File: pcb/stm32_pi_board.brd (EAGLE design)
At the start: 84 x 56 mm, 67 parts, among them IC1 LD1117, IC2 ESP-11, IC3 LD1117, IC4 STM32F405RG, IC5 STF203-22, Q1 BSH205, Q2 N2004, Q5 BSH205, Q6 N2004, X1 PJ-043-SMT, X2 DM3AT, X3 XM7D-0512

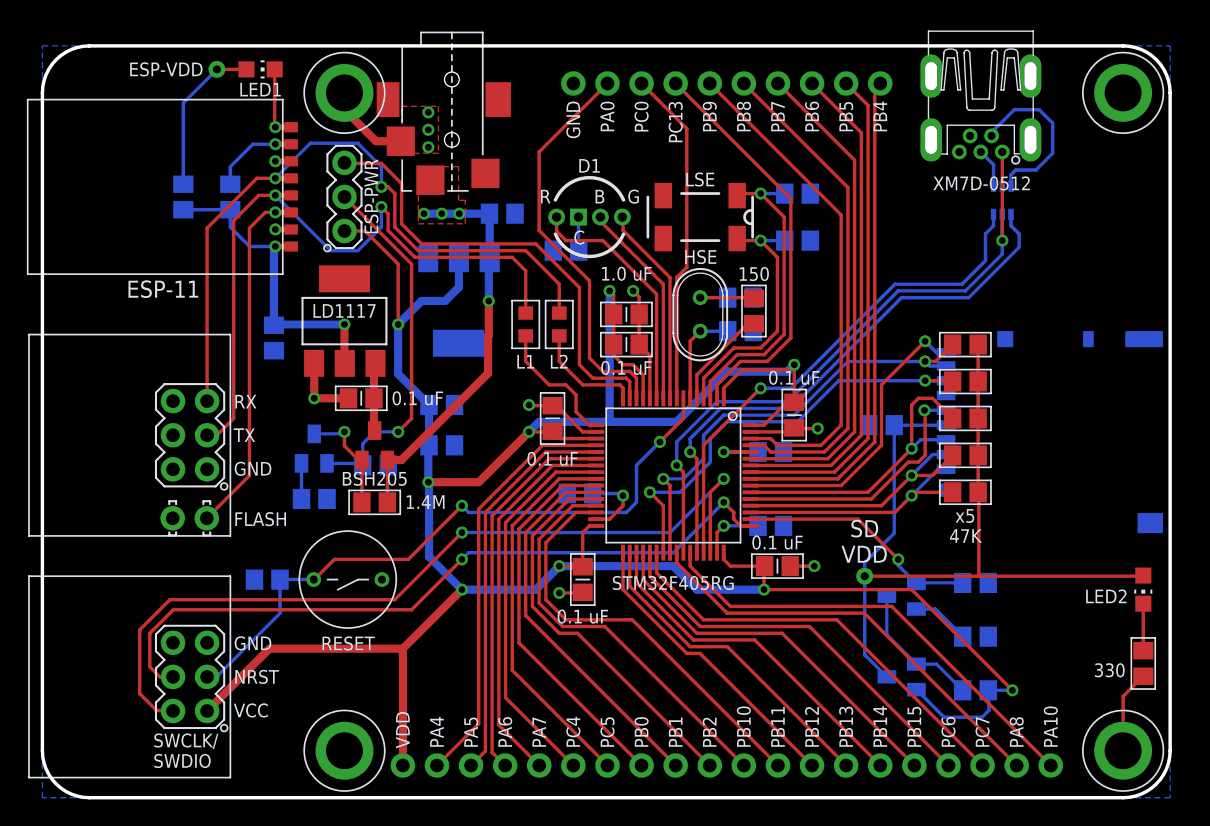
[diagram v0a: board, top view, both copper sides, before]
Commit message: Imprved stm32_pi_board
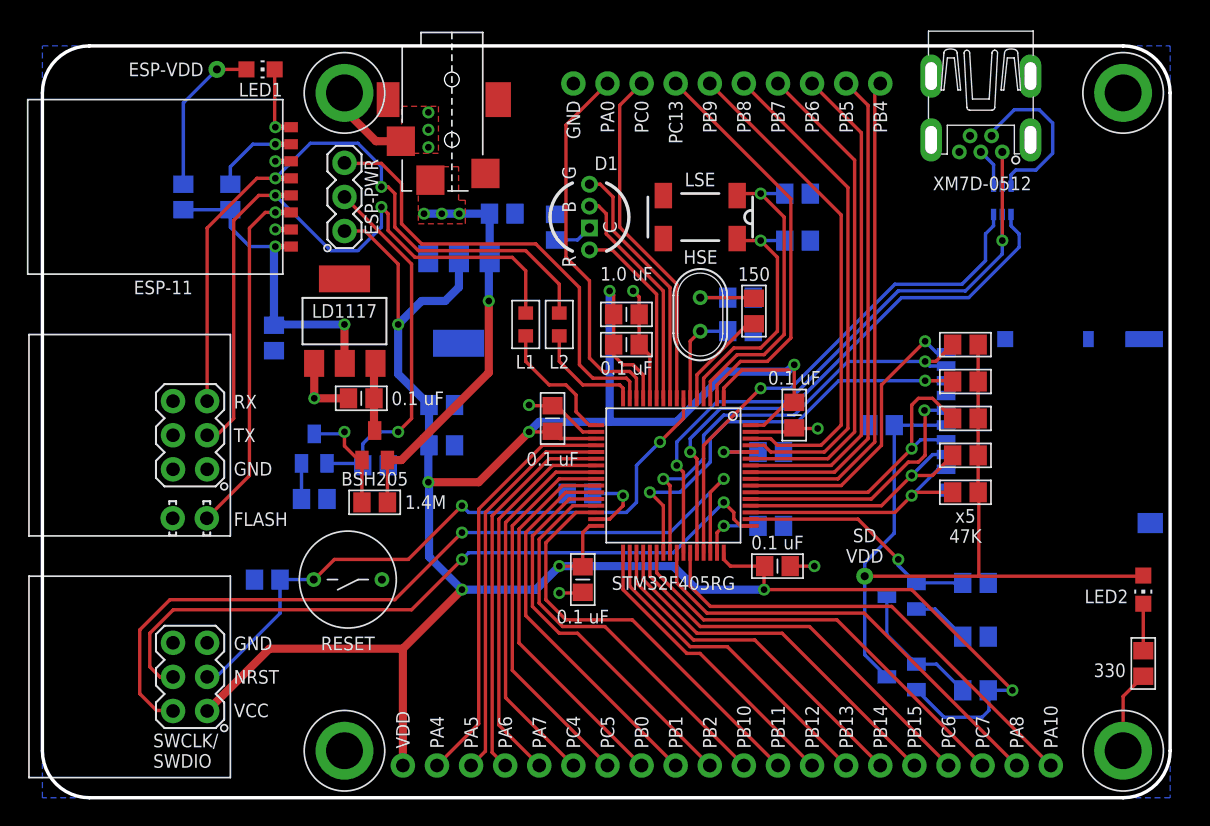
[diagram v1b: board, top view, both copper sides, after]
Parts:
- IC1, IC3: device burr-brown:SOT223 -> MyComponents:SOT223
- SV1, SV2: value (none) -> 75867-331LF
- SV4: value (none) -> 68000-420HLF
- SV5: value (none) -> 69190-410HLF
- moved R6 1.90 mm to (38.2, 42.5), turned to 90 degrees
- turned D1 to 90 degrees
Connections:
- net BOOT1 renamed BOOT
- net N$42 renamed D1_BLUE
- net N$43 renamed D1_RED
- net N$44 renamed D1_GREEN
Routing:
- net D1_RED: track 18.2 -> 14.1 mm
- net D1_GREEN: track 15.0 -> 18.9 mm
- net PA0: track 29.7 -> 28.1 mm
- net D1_BLUE: track 15.5 -> 17.0 mm
- net PA8: track 32.3 -> 33.2 mm
- net PA10: track 34.0 -> 34.9 mm
- net PC0: track 25.2 -> 25.9 mm

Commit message: STM32-Pi Board submitted to factory
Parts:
- moved X3 3.00 mm to (72.9, 49.0)
- moved IC5 1.40 mm to (72.9, 44.5)
- moved SV4 0.50 mm to (51.0, 2.90)
- moved SV5 0.10 mm to (51.0, 53.1)
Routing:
- net N$36: track 12.8 -> 6.27 mm
- net USB-VBUS: track 48.1 -> 49.5 mm
- net USB-DM: track 41.8 -> 42.7 mm
- net USB-DP: track 38.4 -> 38.9 mm
- net PA5: track 29.4 -> 28.9 mm
- net PA4: track 31.1 -> 30.6 mm
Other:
- board text added: "STM32-Pi Board Revision 1.0 (C) Mikhail Kulesh, 2017"

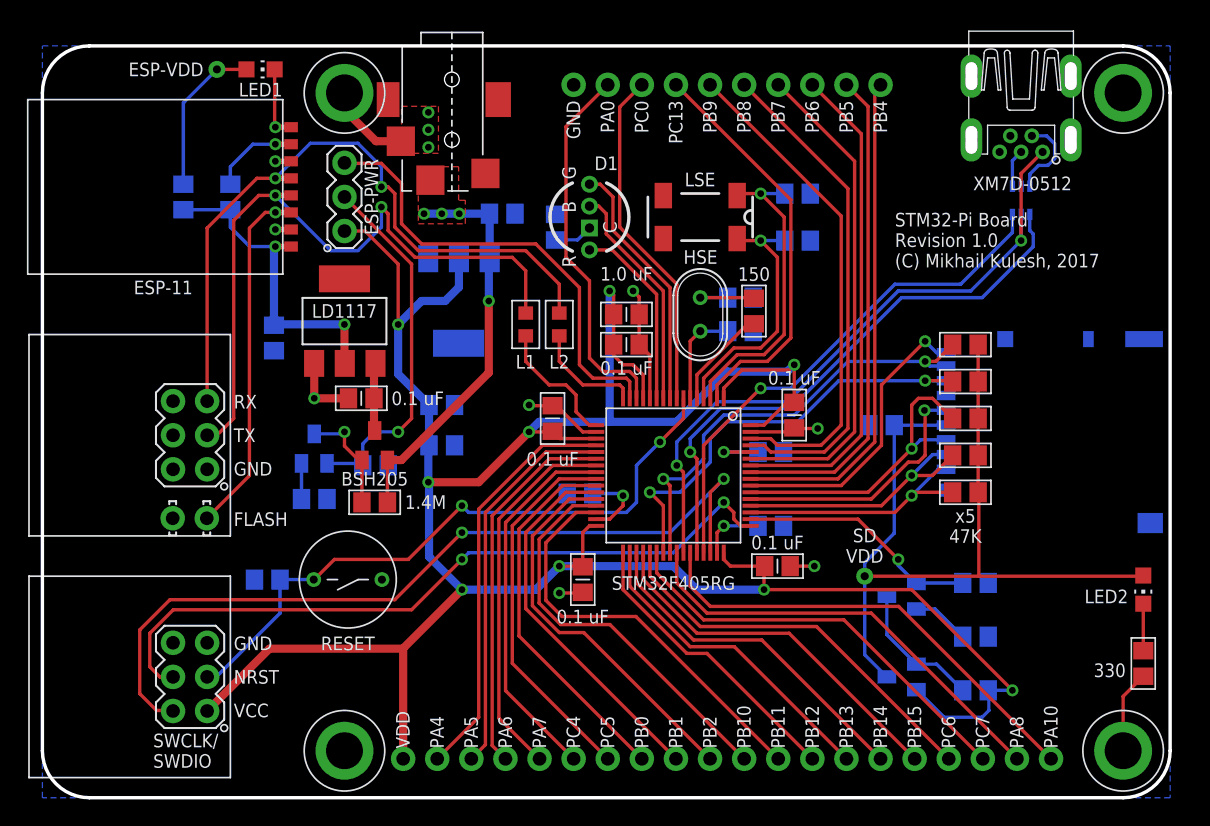
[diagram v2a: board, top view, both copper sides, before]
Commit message: Fixed minor layout bugs
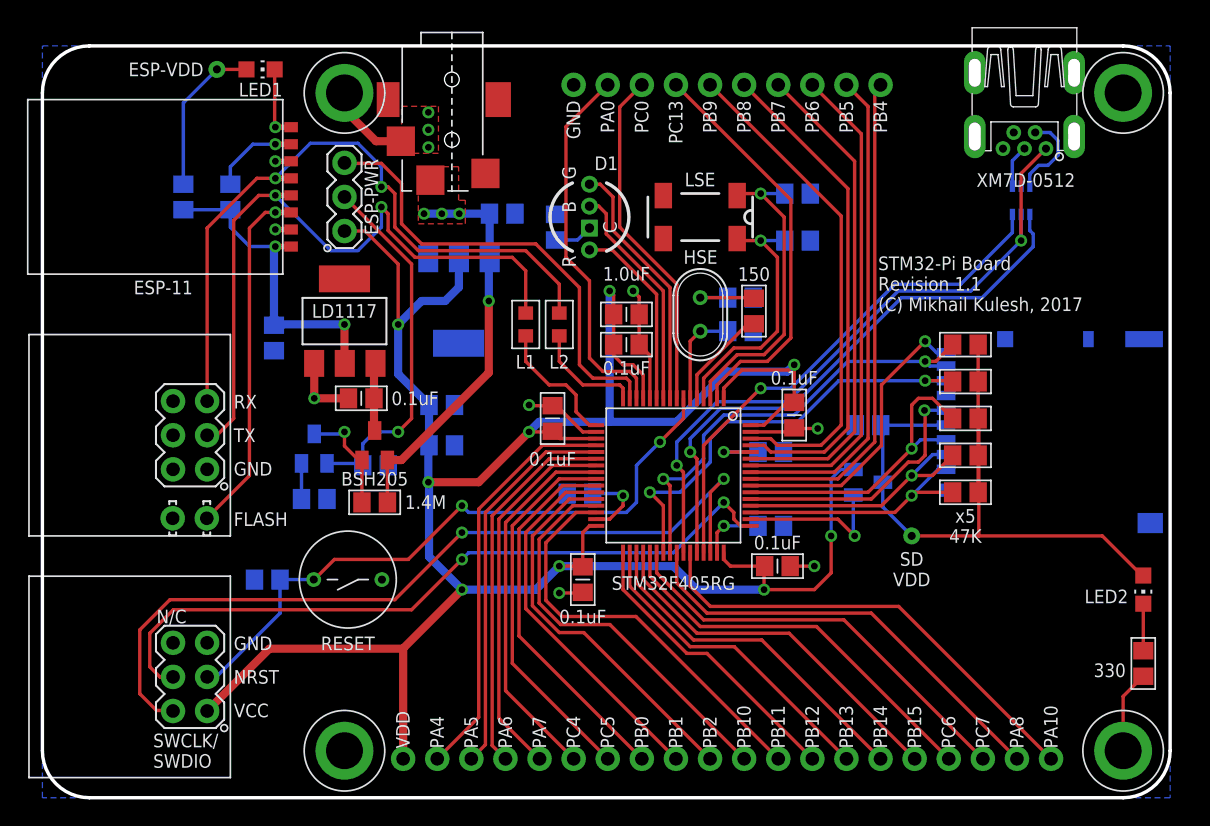
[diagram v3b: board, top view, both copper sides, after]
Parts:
- removed Q6: N2004, MyComponents:SOT23
- removed R11: 330K, MyComponents:R0805
- removed R12: 10K, MyComponents:R0805
- removed R9: 1.4M, MyComponents:R0805
- C10, C11, C12, C16, C19, C2, C6, C8, C9: value 0.1 uF -> 0.1uF
- C13: value 1.0 uF -> 1.0uF
- C17, C18: value 2.2 uF -> 2.2uF
- C3, C7: value 10 uF -> 10uF
- moved Q5 14.7 mm to (61.5, 23.5), turned to 90 degrees
- moved C19 1.00 mm to (61.5, 27.8)
- moved X3 0.35 mm to (73.2, 49.2)
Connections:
- removed net D_VG: Q5.1, Q6.3, R9.1
- removed net N$136: Q6.2, R12.2
- net GND: no longer R11.1, R12.1
- net SD-ON: now also Q5.1; no longer Q6.1, R11.2
- net VDD: no longer R9.2
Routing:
- net VDD: track 205.3 -> 188.4 mm
- net D_VG: track 10.2 -> 0.00 mm
- net SD-VDD: track 62.3 -> 52.5 mm
- net SD-ON: track 18.1 -> 11.4 mm
- net N$136: track 4.30 -> 0.00 mm
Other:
- board text added: "N/C"
- board text added: "STM32-Pi Board Revision 1.1 (C) Mikhail Kulesh, 2017"
- board text removed: "STM32-Pi Board Revision 1.0 (C) Mikhail Kulesh, 2017"

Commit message: Updated PCB
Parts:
- removed SV5: 69190-410HLF, MyComponents:MA10-1-NO-PL
- added SV3: (no value), MyComponents:MA12-1-NO-PL
- moved SV4 0.50 mm to (51.5, 2.90)
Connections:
- net GND: now also SV3.2; no longer SV5.1
- net PA0: now also SV3.3; no longer SV5.2
- net PB4: now also SV3.11; no longer SV5.10
- net PB5: now also SV3.10; no longer SV5.9
- net PB6: now also SV3.9; no longer SV5.8
- net PB7: now also SV3.8; no longer SV5.7
- net PB8: now also SV3.7; no longer SV5.6
- net PB9: now also SV3.6; no longer SV5.5
- net PC0: now also SV3.4; no longer SV5.3
- net PC13: now also SV3.5; no longer SV5.4
- net USB-VBUS: now also SV3.12
- net VIN: now also SV3.1
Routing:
- net VIN: track 31.6 -> 46.3 mm
- net USB-VBUS: track 49.9 -> 64.6 mm
- net ESP-TXI: track 50.7 -> 52.1 mm
- net PB1: track 28.0 -> 29.1 mm
- net PB2: track 29.0 -> 30.0 mm
- net PB10: track 30.1 -> 30.9 mm
- net ESP-RXI: track 51.8 -> 52.5 mm
- net PB11: track 31.2 -> 31.8 mm
- net PC6: track 29.6 -> 30.1 mm
- net PB15: track 27.7 -> 28.2 mm
- net PB14: track 25.9 -> 26.4 mm
- net PB13: track 24.0 -> 24.5 mm
- net PB12: track 22.1 -> 22.6 mm
- net PA8: track 33.0 -> 33.5 mm
- net PA10: track 34.7 -> 35.2 mm
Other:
- board text added: "+3.3V"
- board text added: "+5V"
- board text added: "VBUS"
- board text removed: "VDD"

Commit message: Revision 1.1 submitted to factory
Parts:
- removed ESP-PWR: (no value), MyComponents:MA03-1
- removed IC1: LD1117, MyComponents:SOT223
- removed LED1, LED2: R971, led:CHIP-LED0805
- removed Q1: BSH205, MyComponents:SOT23
- removed Q2: N2004, MyComponents:SOT23
- removed R1: 1.4M, MyComponents:R0805
- removed R2: 330K, MyComponents:R0805
- added ESP-ON, SD-ON: R971, led:CHIP-LED0805
- added IC6: MIC5219-3.3, v-reg-micrel:SOT23-5
- added PWR: (no value), MyComponents:MA03-1
- C2: value 0.1uF -> 470pF
- C3: value 10uF -> 2.2uF
- moved R13 19.2 mm to (82.0, 29.2), turned to 270 degrees
- moved C2 14.3 mm to (12.2, 38.2), flipped to the bottom, turned to 180 degrees
- moved R3 14.0 mm to (12.2, 33.8)
- moved C19 13.3 mm to (74.8, 29.2), flipped to the top, turned to 270 degrees
- moved Q5 13.3 mm to (74.8, 22.0), flipped to the top, turned to 0 degrees
- moved C6 11.9 mm to (23.8, 38.0), flipped to the top, turned to 180 degrees
- moved C3 8.40 mm to (12.2, 41.0), turned to 180 degrees
- moved IC3 8.14 mm to (25.0, 31.5), flipped to the top
- moved C14 3.47 mm to (31.5, 29.2), flipped to the top, turned to 180 degrees
- moved C7 2.85 mm to (31.5, 31.5), flipped to the top, turned to 180 degrees
- moved R5 2.47 mm to (12.2, 46.5), turned to 180 degrees
- moved R4 2.02 mm to (12.2, 43.8), turned to 180 degrees
- moved R6 0.79 mm to (38.0, 43.2)
- moved L1 0.56 mm to (35.8, 34.8)
- moved L2 0.56 mm to (38.2, 34.8)
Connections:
- removed net E_VG: Q1.1, Q2.3, R1.1
- removed net N$148: C2.2, IC1.3, Q1.3
- removed net N$150: Q2.2, R3.2
- new net N$4: C2.2, IC6.4
- net ESP-ON: now also PWR.3; no longer ESP-PWR.3
- net ESP-ON1: now also IC6.3, PWR.2, R3.2; no longer ESP-PWR.2, Q2.1, R2.2
- net ESP-VDD: now also IC6.5; no longer IC1.2
- net GND: now also ESP-ON.C, IC6.2; no longer IC1.1, LED1.C, R2.1
- net N$10: now also ESP-ON.A; no longer LED1.A
- net N$120: now also SD-ON.C; no longer LED2.C
- net SD-VDD: now also SD-ON.A; no longer LED2.A
- net VDD: now also PWR.1; no longer ESP-PWR.1
- net VIN: now also IC6.1; no longer Q1.2, R1.2
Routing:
- net VDD: track 188.6 -> 222.3 mm, vias 9 -> 8
- net GND: track 46.4 -> 68.9 mm, vias 10 -> 9
- net SD-VDD: track 52.5 -> 34.7 mm
- net ESP-ON1: track 27.3 -> 44.5 mm
- net ESP-VDD: track 24.1 -> 13.2 mm, vias 2 -> 1
- net SD-ON: track 11.4 -> 21.2 mm, vias 1 -> 0
- net ESP-ON: track 34.4 -> 43.9 mm
- net E_VG: track 8.25 -> 0.00 mm, vias 1 -> 0
- net VIN: track 46.3 -> 38.3 mm
- net ESP-TXI: track 52.1 -> 44.3 mm, vias 2 -> 1
- net ESP-RXI: track 52.5 -> 45.7 mm, vias 2 -> 1
- net N$148: track 5.07 -> 0.00 mm
- net N$10: track 11.8 -> 15.9 mm
- net N$4: track 0.00 -> 3.51 mm
- net USB-VBUS: track 64.6 -> 68.0 mm
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- removed copper zone on layer 1, net GND
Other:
- board text removed: "ESP-VDD"
- board text removed: "SD VDD"

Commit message: Assembled board 1.2
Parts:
- added C20, C21, C25, C26, C28, C29, C30, C31, C33: 0.1uF, MyComponents:C0805
- added C22: 2.2uF, MyComponents:CPOL0805
- added C23: 470pF, MyComponents:C0805
- added C24, C27, C35, C36, C37: 47uF, MyComponents:CPOL1311
- added C32, C34: 1.0uF, MyComponents:C0805
- added IC1, IC8: MIC5219-3.3, MyComponents:SOT23-5
- added IC7: IS31AP2005, MyComponents:MSOP-8
- added IC9: UDA1334ATS, MyComponents:SSOP16
- added Q1: FDG6332C, MyComponents:SC70-6
- added R1, R2, R20, R21, R9: 150K, MyComponents:R0805
- added R11: 6.7K, MyComponents:R0805
- added R12, R18: 1, MyComponents:R0805
- added R19, R24, R25: 10K, MyComponents:R0805
- added R22, R23: 220K, MyComponents:R0805
- added SV5: (no value), MyComponents:MA04-1
- C3: device MyComponents:C0805 -> MyComponents:CPOL0805
- C6: value 0.1uF -> 470pF
- C7: value 10uF -> 2.2uF; device MyComponents:C0805 -> MyComponents:CPOL0805
- HSE: device MyComponents:HC-46X -> MyComponents:Q-FA-128
- IC3: value LD1117 -> IS31AP2005; device MyComponents:SOT223 -> MyComponents:MSOP-8
- IC6: device v-reg-micrel:SOT23-5 -> MyComponents:SOT23-5
- LSE: device MyComponents:MC-306 -> MyComponents:Q-CM7V-T1A
- R7: value 150 -> 100
- moved C16 63.7 mm to (80.0, 9.00), flipped to the top
- moved SV1 60.5 mm to (71.2, 14.5), turned to 270 degrees
- moved RESET 57.3 mm to (80.0, 14.5)
- moved IC3 26.9 mm to (11.0, 8.50), turned to 90 degrees
- moved L2 19.4 mm to (22.2, 45.8), turned to 0 degrees
- moved ESPJ2 17.1 mm to (3.81, 36.8), turned to 180 degrees
- moved FLASH 17.1 mm to (6.35, 36.8), turned to 180 degrees
- moved L1 16.0 mm to (22.2, 43.2), turned to 0 degrees
- moved LSE 11.3 mm to (57.0, 35.2)
- moved C6 11.0 mm to (33.8, 33.5), flipped to the bottom
- moved C17 6.76 mm to (37.2, 16.5), flipped to the top, turned to 90 degrees
- moved C14 6.37 mm to (37.5, 31.4), turned to 0 degrees
- moved C4 6.32 mm to (58.2, 39.0), flipped to the top, turned to 270 degrees
- moved R8 6.06 mm to (56.5, 31.4), flipped to the top, turned to 0 degrees
- moved C7 5.03 mm to (33.8, 27.0), flipped to the bottom, turned to 0 degrees
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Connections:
- removed net PB10: IC4.29, SV4.10
- removed net PB11: IC4.30, SV4.9
- removed net PB12: IC4.33, SV4.8
- removed net PB13: IC4.34, SV4.7
- removed net PB14: IC4.35, SV4.6
- removed net PB15: IC4.36, SV4.5
- new net AUD-BCK: IC4.29, IC9.1, SV4.10
- new net AUD-DAT: IC4.36, IC9.3, SV4.5
- new net AUD-L: C35.1+, IC9.14
- new net AUD-MUTE: IC4.34, IC9.8, R19.1, SV4.7
- new net AUD-ON: IC4.30, IC8.3, Q1.2, R24.1, SV4.9
- new net AUD-R: C36.1+, IC9.16
- new net AUD-REF: C24.1+, C25.1, IC9.12, R11.1, R9.2
- new net AUD-SMPL: IC4.35, IC9.6, SV4.6
- new net AUD-WS: IC4.33, IC9.2, SV4.8
- new net N$11: IC3.8, SV5.1
- new net N$13: IC3.5, SV5.2
- new net N$17: C20.1, R1.2
- new net N$22: IC7.8, SV5.3
- new net N$24: IC7.5, SV5.4
- new net N$26: IC3.3, R1.1
- new net N$27: IC7.3, R2.1
- new net N$37: C21.1, R2.2
- new net N$38: IC3.4, R20.1
- new net N$42: C28.1, C37.1+, IC9.4, R18.1
- new net N$43: IC7.4, R21.1
- new net N$44: C23.2, IC8.4
- new net N$46: C26.1, C27.1+, IC9.13, R12.1
- new net N$47: C30.1, R21.2
- new net N$5: C6.2, IC1.4
- new net N$65: C29.1, R20.2
- new net N$69: C29.2, C35.2-, R22.2
- new net N$70: Q1.3, R18.2
- new net N$72: C30.2, C36.2-, R23.2
- new net N$86: Q1.5, Q1.6, R25.2
- new net VSS: C22.1+, C31.1, C32.1, C33.1, C34.1, IC3.1, IC3.6, IC7.1, IC7.6, IC8.5, R12.2, R9.1
- net ESP-VDD: now also C3.1+; no longer C3.2
- net GND: now also C20.2, C21.2, C22.2-, C23.1, C24.2-, C25.2, C26.2, C27.2-, C28.2, C3.2-, C31.2, C32.2, C33.2, C34.2, C37.2-, C7.2-, IC1.2, IC3.7, IC7.7, IC8.2, IC9.10, IC9.11, IC9.15, IC9.5, IC9.7, IC9.9, Q1.1, R11.2, R19.2, R22.1, R23.1, R24.2; no longer C3.1, C7.1, IC3.1
- net N$78: now also HSE.3; no longer HSE.2
- net Q2P: now also LSE.2; no longer LSE.4
- net VDD: now also C7.1+, IC1.5, Q1.4, R25.1; no longer C7.2, IC3.2, PWR.1
- net VIN: now also IC1.1, IC1.3, IC8.1, PWR.1; no longer C6.2, IC3.3
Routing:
- net VDD: track 222.3 -> 146.9 mm, vias 8 -> 6
- net AUD-ON: track 0.00 -> 62.6 mm, vias 0 -> 3
- net AUD-SMPL: track 0.00 -> 47.7 mm, vias 0 -> 1
- net AUD-MUTE: track 0.00 -> 47.0 mm, vias 0 -> 1
- net AUD-DAT: track 0.00 -> 45.2 mm, vias 0 -> 1
- net AUD-BCK: track 0.00 -> 40.0 mm, vias 0 -> 1
- net AUD-WS: track 0.00 -> 39.8 mm, vias 0 -> 1
- net VSS: track 0.00 -> 33.4 mm, vias 0 -> 3
- net GND: track 68.9 -> 101.3 mm, vias 9 -> 19
- net SWCLK: track 54.3 -> 22.2 mm, vias 2 -> 0
- net PB11: track 31.8 -> 0.00 mm
- net PB10: track 30.9 -> 0.00 mm
- net PB15: track 28.2 -> 0.00 mm
- net PB14: track 26.4 -> 0.00 mm
- net SWDIO: track 61.8 -> 36.6 mm, vias 2 -> 0
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- added copper zone on layer 1, net GND
- added copper zone on layer 1, net VSS
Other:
- board text added: "A+"
- board text added: "A-"
- board text added: "CL"
- board text added: "D+"
- board text added: "D-"
- board text added: "D-class ampl"
- board text added: "IO"
- board text added: "L"
- board text added: "NC"
- board text added: "R"
- board text added: "STM32-Pi Board Revision 1.2 (C) Mikhail Kulesh"
- board text added: "SWD"
- board text added: "audio-DAC"
- board text added: "micro-SD"
- board text added: "x2"
- board text added: "x4"
- board text removed: "N/C"
- board text removed: "STM32-Pi Board Revision 1.1 (C) Mikhail Kulesh, 2017"
- board text removed: "SWCLK/ SWDIO"
